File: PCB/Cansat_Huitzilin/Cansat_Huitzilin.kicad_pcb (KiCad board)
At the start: 4 copper layers, 59 x 59 mm, 72 parts, among them IC1 AP64501SP-13, IC2 114993390, IC3 BMM350, IC4 BMI323, IC5 STCC4-D-R3, IC6 SHT40-AD1B-R2, J1 Screw_Terminal_01x02, J2 Conn_01x04, J3 Conn_01x03, J4 Conn_01x06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

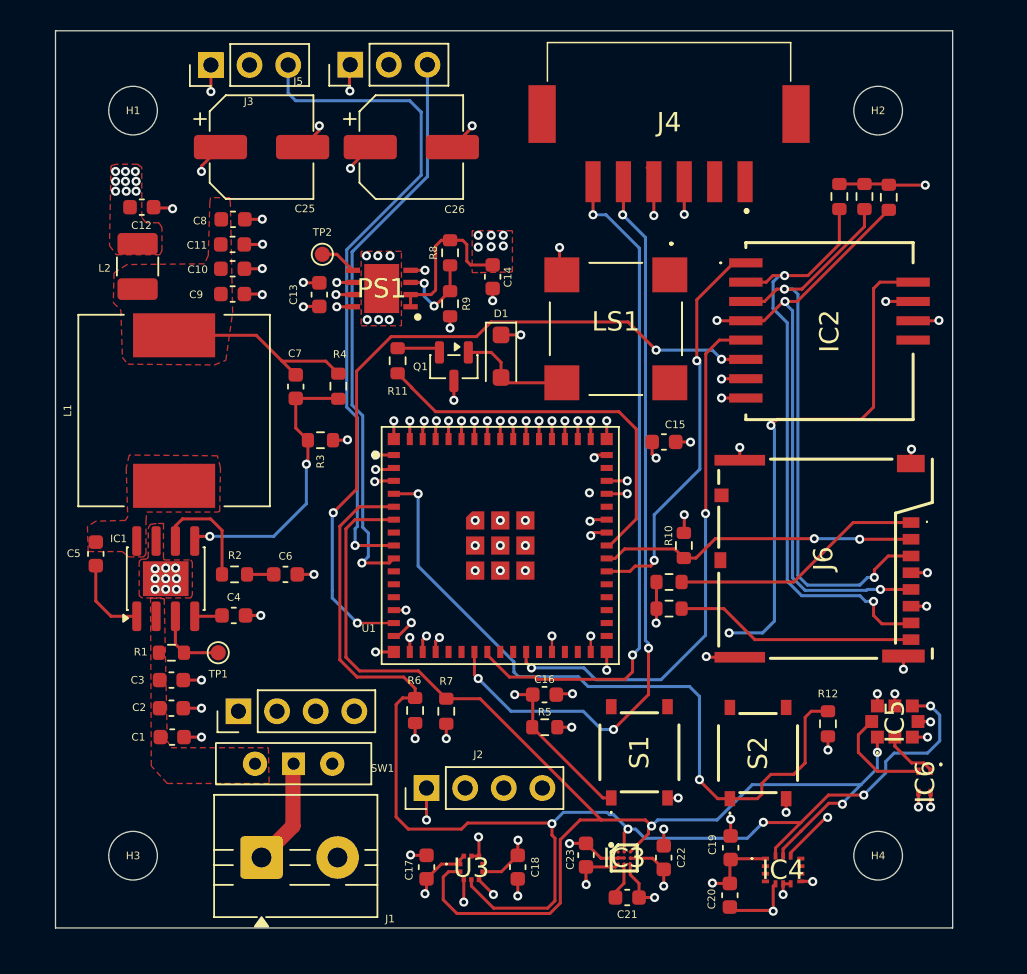
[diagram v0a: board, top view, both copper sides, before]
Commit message: PCB
adding the final serigraphy
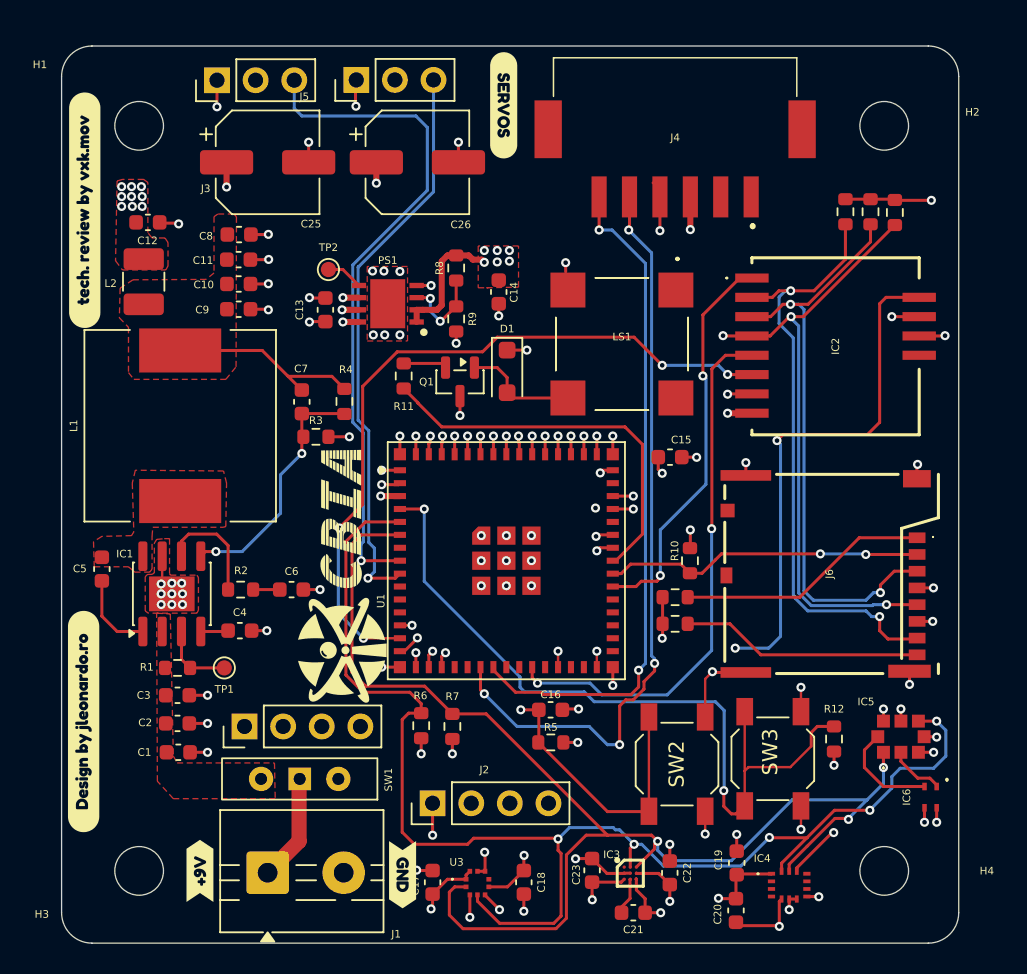
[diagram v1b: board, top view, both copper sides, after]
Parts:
- removed S1, S2: PTS526SM15SMTR2_LFS, SamacSys_Parts:PTS526SM15SMTR2LFS
- added G***: LOGO, LOGO, F.Cu at (89.5, 72.6)
- added G***: LOGO, LOGO, B.Cu at (123.0, 69.3)
- added G***: LOGO, LOGO, B.Cu at (100.3, 63.2)
- added SW2: SW_Push, Button_Switch_SMD:SW_SPST_SKQG_WithoutStem, F.Cu at (111.5, 85.2)
- added SW3: SW_Push, Button_Switch_SMD:SW_SPST_SKQG_WithoutStem, F.Cu at (117.8, 84.9)
- added kibuzzard-69ACDBDC: G***, kibuzzard-69ACDBDC, F.Cu at (100.1, 41.9)
- added kibuzzard-69ACDC11: G***, kibuzzard-69ACDC11, F.Cu at (80.1, 92.2)
- added kibuzzard-69ACDC24: G***, kibuzzard-69ACDC24, F.Cu at (93.4, 92.5)
- added kibuzzard-69ACDC57: G***, kibuzzard-69ACDC57, F.Cu at (72.5, 82.4)
- added kibuzzard-69ACDC7E: G***, kibuzzard-69ACDC7E, F.Cu at (72.5, 48.8)
- added kibuzzard-69ACDEB2: G***, kibuzzard-69ACDEB2, B.Cu at (86.3, 43.2)
- added kibuzzard-69ACDEB2: G***, kibuzzard-69ACDEB2, B.Cu at (95.5, 43.4)
- added kibuzzard-69ACDECD: G***, kibuzzard-69ACDECD, B.Cu at (93.1, 43.4)
- added kibuzzard-69ACDECD: G***, kibuzzard-69ACDECD, B.Cu at (83.9, 43.2)
- moved C10 1.08 mm to (82.7, 53.6)
- moved C14 1.08 mm to (99.8, 54.2)
- moved C15 1.08 mm to (111.0, 65.0)
- moved C16 1.08 mm to (103.2, 81.7)
- moved C17 1.08 mm to (95.4, 93.0)
- moved C18 1.08 mm to (101.4, 93.0)
- moved C19 1.08 mm to (115.4, 91.7)
- moved C2 1.08 mm to (78.6, 82.5)
- moved C22 1.08 mm to (111.0, 92.4)
- moved C23 1.08 mm to (105.9, 92.2)
- moved C26 1.08 mm to (94.4, 45.6)
- moved C3 1.08 mm to (78.6, 80.7)
- moved C5 1.08 mm to (73.7, 72.4)
- moved C6 1.08 mm to (86.1, 73.8)
- moved C9 1.08 mm to (82.7, 55.3)
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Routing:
- net Enable ESP: track 31.9 -> 40.1 mm
- net GND: track 94.2 -> 101.7 mm, vias 93 -> 94
- net BOOT: track 47.8 -> 52.6 mm
- net +3.3V: track 57.0 -> 54.9 mm
- net Net-(IC1-FB): track 18.4 -> 16.3 mm
- net SCL: track 83.2 -> 84.6 mm
- net +4V: track 12.3 -> 11.3 mm
- net SDA: track 88.7 -> 89.3 mm
- added copper zone on F.Cu, net BOOT
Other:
- outline, holes or cut-outs redrawn
